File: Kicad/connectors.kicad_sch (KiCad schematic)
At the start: 13 parts, among them J1 Connecteur batterie, J10 HM_10_BLE_Module, J11 DFPlayer_Left, J12 DFPlayer_Right, J14 Speaker, J2 Motor_Left, J3 Motor_Right, J4 Servo_Left, J5 MPU-6050, J6 APDS9960, J7 VL53L0CXV0DH - TOF, J8 Servo_Right, J9 Neopixel

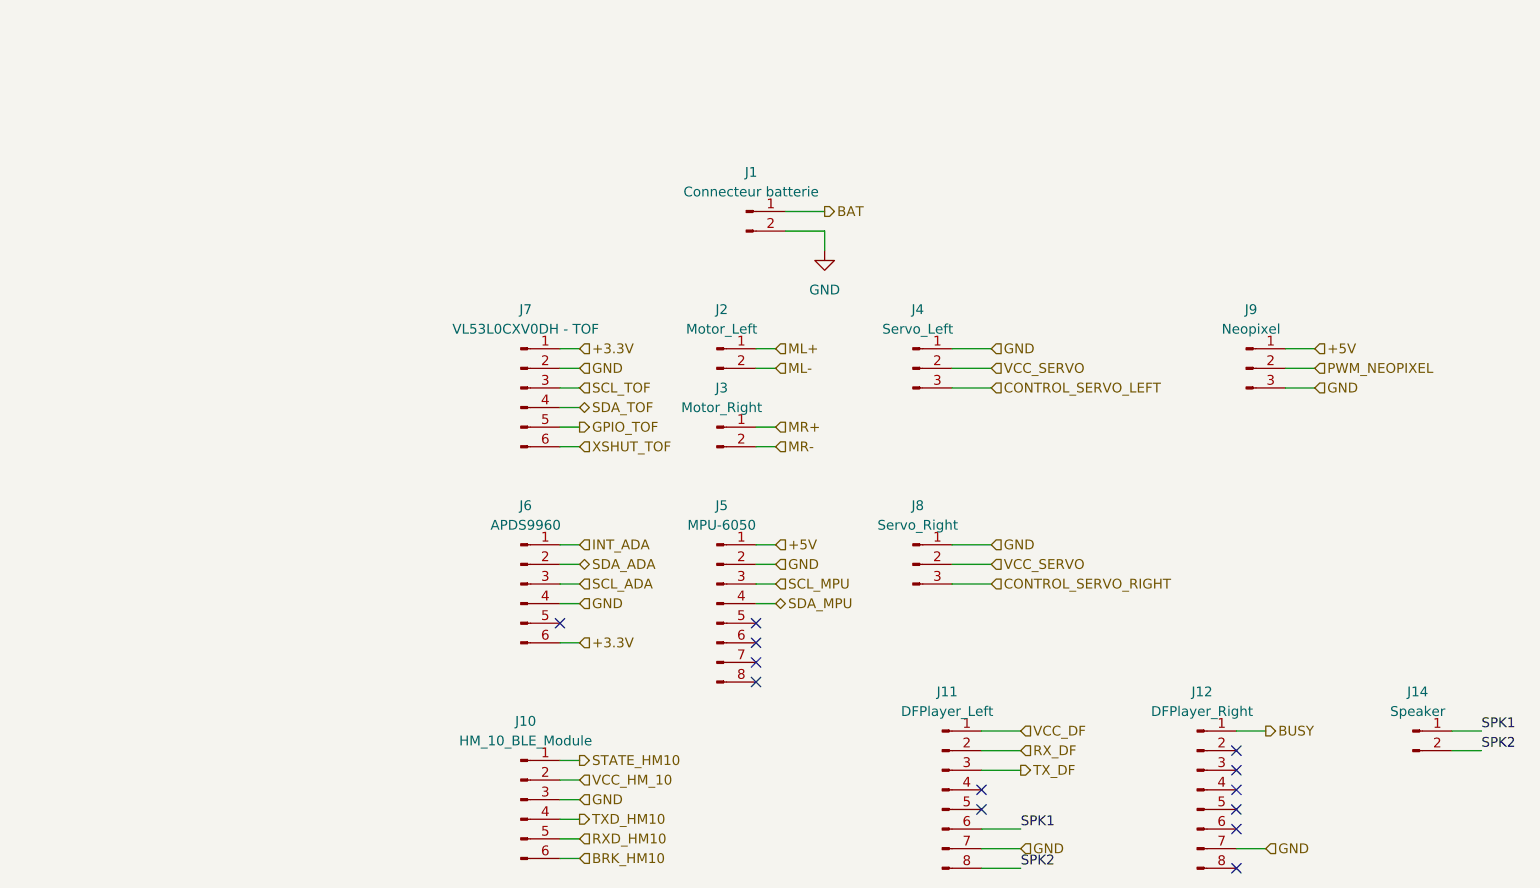
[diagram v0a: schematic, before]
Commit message: Feat: Added power LEDs 5v and 3v, Added Jumpers to battery and bms, Added segmentation in connector sheet, Added encoders, Changed page name from motor diver right to motor driver, Redid annotations, Changed output organisation on stm to match new ioc
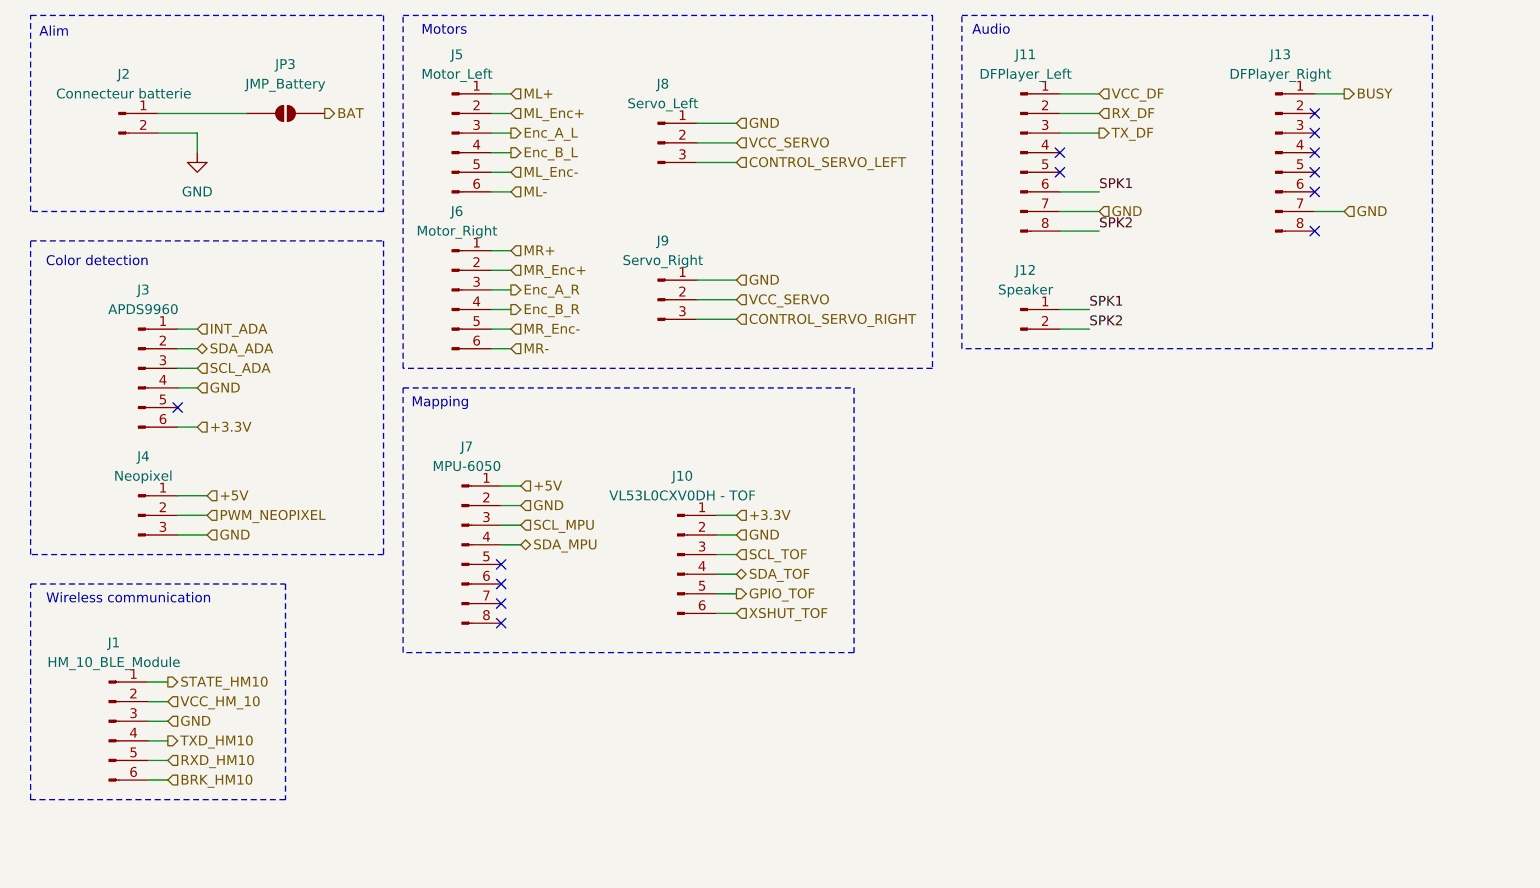
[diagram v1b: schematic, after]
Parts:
- removed J2: Motor_Left, Connector_JST:JST_ZH_B2B-ZR_1x02_P1.50mm_Vertical, symbol Connector:Conn_01x02_Pin
- removed J3: Motor_Right, Connector_JST:JST_ZH_B2B-ZR_1x02_P1.50mm_Vertical, symbol Connector:Conn_01x02_Pin
- added J5: Motor_Left, symbol Connector:Conn_01x06_Pin
- added J6: Motor_Right, symbol Connector:Conn_01x06_Pin
- added JP3: JMP_Battery, symbol Jumper:SolderJumper_2_Open
- renumbered J10 to J1, J7 to J10, J14 to J12, J12 to J13, J1 to J2, J6 to J3, J9 to J4, J5 to J7, J4 to J8, J8 to J9
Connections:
- net BAT: now also JP3.2 (B); no longer J2.1 (Pin_1)
- net ML+: now also J5.1 (Pin_1)
- net ML-: now also J5.6 (Pin_6)
- net MR+: now also J6.1 (Pin_1)
- net MR-: now also J6.6 (Pin_6)
- new net: J2.1 (Pin_1), JP3.1 (A)
- new net Enc_A_L: J5.3 (Pin_3)
- new net Enc_A_R: J6.3 (Pin_3)
- new net Enc_B_L: J5.4 (Pin_4)
- new net Enc_B_R: J6.4 (Pin_4)
- new net ML_Enc+: J5.2 (Pin_2)
- new net ML_Enc-: J5.5 (Pin_5)
- new net MR_Enc+: J6.2 (Pin_2)
- new net MR_Enc-: J6.5 (Pin_5)
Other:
- note added: "Alim"
- note added: "Audio"
- note added: "Color detection"
- note added: "Mapping"
- note added: "Motors"
- note added: "Wireless communication"
- moved on the sheet: J1, J10, J11, J12, J13, J2, J3, J4, J7, J8, J9

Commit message: feat: added the footprints for the solderjumpers
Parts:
- JP3: footprint (none) -> Jumper:SolderJumper-2_P1.3mm_Open_TrianglePad1.0x1.5mm
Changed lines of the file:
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@@
 			)
 		)
-		(property "Footprint" ""
+		(property "Footprint" "Jumper:SolderJumper-2_P1.3mm_Open_TrianglePad1.0x1.5mm"
 			(at 52.07 33.02 0)
 			(hide yes)

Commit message: feat: replaced the footprints of the connectors with fooprints of JST connectors
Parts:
- J10: footprint Connector_PinSocket_2.54mm:PinSocket_1x06_P2.54mm_Vertical -> Connector_JST:JST_XH_S6B-XH-A_1x06_P2.50mm_Horizontal
- J11, J13, J7: footprint Connector_PinSocket_2.54mm:PinSocket_1x08_P2.54mm_Vertical -> Connector_JST:JST_XH_B8B-XH-A_1x08_P2.50mm_Vertical
- J12: footprint Connector_PinSocket_2.54mm:PinSocket_1x02_P2.54mm_Vertical -> Connector_JST:JST_XH_B2B-XH-A_1x02_P2.50mm_Vertical
- J3: footprint Connector_PinSocket_2.54mm:PinSocket_1x06_P2.54mm_Vertical -> Connector_JST:JST_XH_B6B-XH-A_1x06_P2.50mm_Vertical
- J4, J8, J9: footprint Connector_PinHeader_2.54mm:PinHeader_1x03_P2.54mm_Vertical -> Connector_JST:JST_XH_B3B-XH-A_1x03_P2.50mm_Vertical
- J5, J6: footprint (none) -> Connector_JST:JST_XH_B2B-XH-A_1x02_P2.50mm_Vertical
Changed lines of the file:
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@@
 			)
 		)
-		(property "Footprint" "Connector_PinSocket_2.54mm:PinSocket_1x08_P2.54mm_Vertical"
+		(property "Footprint" "Connector_JST:JST_XH_B8B-XH-A_1x08_P2.50mm_Vertical"
 			(at 74.93 88.9 0)
 			(hide yes)
@@
 			)
 		)
-		(property "Footprint" "Connector_PinHeader_2.54mm:PinHeader_1x03_P2.54mm_Vertical"
+		(property "Footprint" "Connector_JST:JST_XH_B3B-XH-A_1x03_P2.50mm_Vertical"
 			(at 100.33 36.83 0)
 			(hide yes)
@@
 			)
 		)
-		(property "Footprint" "Connector_PinSocket_2.54mm:PinSocket_1x08_P2.54mm_Vertical"
+		(property "Footprint" "Connector_JST:JST_XH_B8B-XH-A_1x08_P2.50mm_Vertical"
 			(at 180.34 38.1 0)
 			(hide yes)
@@
 			)
 		)
-		(property "Footprint" "Connector_PinHeader_2.54mm:PinHeader_1x03_P2.54mm_Vertical"
+		(property "Footprint" "Connector_JST:JST_XH_B3B-XH-A_1x03_P2.50mm_Vertical"
 			(at 33.02 85.09 0)
 			(hide yes)
@@
 			)
 		)
-		(property "Footprint" "Connector_PinSocket_2.54mm:PinSocket_1x08_P2.54mm_Vertical"
+		(property "Footprint" "Connector_JST:JST_XH_B8B-XH-A_1x08_P2.50mm_Vertical"
 			(at 147.32 38.1 0)
 			(hide yes)
@@
 			)
 		)
-		(property "Footprint" ""
+		(property "Footprint" "Connector_JST:JST_XH_B2B-XH-A_1x02_P2.50mm_Vertical"
 			(at 73.66 35.56 0)
 			(hide yes)
@@
 			)
 		)
-		(property "Footprint" "Connector_PinSocket_2.54mm:PinSocket_1x06_P2.54mm_Vertical"
+		(property "Footprint" "Connector_JST:JST_XH_B6B-XH-A_1x06_P2.50mm_Vertical"
 			(at 33.02 66.04 0)
 			(hide yes)
@@
 			)
 		)
-		(property "Footprint" "Connector_PinSocket_2.54mm:PinSocket_1x02_P2.54mm_Vertical"
+		(property "Footprint" "Connector_JST:JST_XH_B2B-XH-A_1x02_P2.50mm_Vertical"
 			(at 147.32 58.42 0)
 			(hide yes)
@@
 			)
 		)
-		(property "Footprint" "Connector_PinHeader_2.54mm:PinHeader_1x03_P2.54mm_Vertical"
+		(property "Footprint" "Connector_JST:JST_XH_B3B-XH-A_1x03_P2.50mm_Vertical"
 			(at 100.33 57.15 0)
 			(hide yes)
@@
 			)
 		)
-		(property "Footprint" ""
+		(property "Footprint" "Connector_JST:JST_XH_B2B-XH-A_1x02_P2.50mm_Vertical"
 			(at 73.66 55.88 0)
 			(hide yes)
@@
 			)
 		)
-		(property "Footprint" "Connector_PinSocket_2.54mm:PinSocket_1x06_P2.54mm_Vertical"
+		(property "Footprint" "Connector_JST:JST_XH_S6B-XH-A_1x06_P2.50mm_Horizontal"
 			(at 102.87 90.17 0)
 			(hide yes)

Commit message: feat: changed the footprints to 1206 for the shunt resistors R18 and R19 and put a JST connector footprint for the Bluetooth Module
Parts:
- J1: footprint Connector_PinSocket_2.54mm:PinSocket_1x06_P2.54mm_Vertical -> Connector_JST:JST_XH_S6B-XH-A_1x06_P2.50mm_Horizontal
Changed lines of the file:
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@@
 			)
 		)
-		(property "Footprint" "Connector_PinSocket_2.54mm:PinSocket_1x06_P2.54mm_Vertical"
+		(property "Footprint" "Connector_JST:JST_XH_S6B-XH-A_1x06_P2.50mm_Horizontal"
 			(at 29.21 111.76 0)
 			(hide yes)

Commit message: fix: replaced the fooprints of the connectors of the TOF and Bluetooth Module with vertical ones
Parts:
- J1, J10: footprint Connector_JST:JST_XH_S6B-XH-A_1x06_P2.50mm_Horizontal -> Connector_JST:JST_XH_B6B-XH-A_1x06_P2.50mm_Vertical
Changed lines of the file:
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@@
 			)
 		)
-		(property "Footprint" "Connector_JST:JST_XH_S6B-XH-A_1x06_P2.50mm_Horizontal"
+		(property "Footprint" "Connector_JST:JST_XH_B6B-XH-A_1x06_P2.50mm_Vertical"
 			(at 29.21 111.76 0)
 			(hide yes)
@@
 			)
 		)
-		(property "Footprint" "Connector_JST:JST_XH_S6B-XH-A_1x06_P2.50mm_Horizontal"
+		(property "Footprint" "Connector_JST:JST_XH_B6B-XH-A_1x06_P2.50mm_Vertical"
 			(at 102.87 90.17 0)
 			(hide yes)

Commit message: feat: electrical schematic validated
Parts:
- removed J2: Connecteur batterie, Connector_JST:JST_XH_B2B-XH-A_1x02_P2.50mm_Vertical, symbol Connector:Conn_01x02_Pin
- removed JP3: JMP_Battery, Jumper:SolderJumper-2_P1.3mm_Open_TrianglePad1.0x1.5mm, symbol Jumper:SolderJumper_2_Open
- added C35, C36, C37, C38, C39, C40, C41, C42, C43, C44: 100n, Capacitor_SMD:C_0402_1005Metric, symbol Device:C_Small
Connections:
- net ML_Enc+ is gone; now on net +3.3V: J5.2 (Pin_2)
- net ML_Enc- is gone; now on net GND: J5.5 (Pin_5)
- net MR_Enc+ is gone; now on net +3.3V: J6.2 (Pin_2)
- net MR_Enc- is gone; now on net GND: J6.5 (Pin_5)
- net VCC_DF is gone; now on net +5V: J11.1 (Pin_1)
- net VCC_HM_10 is gone; now on net +5V: J1.2 (Pin_2)
- net VCC_SERVO is gone; now on net +5V: J8.2 (Pin_2), J9.2 (Pin_2)
- net +3.3V: now also C36.2, C39.1, C41.1, C44.1
- net +5V: now also C35.1, C37.1, C38.1, C40.2, C42.2, C43.1
- net GND: now also C35.2, C36.1, C37.2, C38.2, C39.2, C40.1, C41.2, C42.1, C43.2, C44.2
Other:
- note removed: "Alim"
- moved on the sheet: J1, J3, J4

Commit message: feat: added the footprints for new components and started assigning the JLCPCB part numbers
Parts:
- C35, C36, C37, C38, C39, C40, C41, C42, C43, C44: JLCPCB Part # (none) -> C1525
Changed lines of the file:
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@@
 			)
 		)
+		(property "JLCPCB Part #" "C1525"
+			(at 166.37 41.91 0)
+			(hide yes)
+			(show_name no)
+			(do_not_autoplace no)
+			(effects
+				(font
+					(size 1.27 1.27)
+				)
+			)
+		)
 		(pin "1"
 		)
@@
 			)
 		)
+		(property "JLCPCB Part #" "C1525"
+			(at 92.71 36.83 0)
+			(hide yes)
+			(show_name no)
+			(do_not_autoplace no)
+			(effects
+				(font
+					(size 1.27 1.27)
+				)
+			)
+		)
 		(pin "1"
 		)
@@
 			)
 		)
+		(property "JLCPCB Part #" "C1525"
+			(at 92.71 57.15 0)
+			(hide yes)
+			(show_name no)
+			(do_not_autoplace no)
+			(effects
+				(font
+					(size 1.27 1.27)
+				)
+			)
+		)
 		(pin "1"
 		)
@@
 			)
 		)
+		(property "JLCPCB Part #" "C1525"
+			(at 124.46 87.63 0)
+			(hide yes)
+			(show_name no)
+			(do_not_autoplace no)
+			(effects
+				(font
+					(size 1.27 1.27)
+				)
+			)
+		)
 		(pin "1"
 		)
@@
 			)
 		)
+		(property "JLCPCB Part #" "C1525"
+			(at 35.56 41.91 0)
+			(hide yes)
+			(show_name no)
+			(do_not_autoplace no)
+			(effects
+				(font
+					(size 1.27 1.27)
+				)
+			)
+		)
 		(pin "1"
 		)
@@
 			)
 		)
+		(property "JLCPCB Part #" "C1525"
+			(at 53.34 83.82 0)
+			(hide yes)
+			(show_name no)
+			(do_not_autoplace no)
+			(effects
+				(font
+					(size 1.27 1.27)
+				)
+			)
+		)
 		(pin "1"
 		)
@@
 			)
 		)
+		(property "JLCPCB Part #" "C1525"
+			(at 111.6439 54.61 0)
+			(hide yes)
+			(show_name no)
+			(do_not_autoplace no)
+			(effects
+				(font
+					(size 1.27 1.27)
+				)
+			)
+		)
 		(pin "1"
 		)
@@
 			)
 		)
+		(property "JLCPCB Part #" "C1525"
+			(at 83.82 81.28 0)
+			(hide yes)
+			(show_name no)
+			(do_not_autoplace no)
+			(effects
+				(font
+					(size 1.27 1.27)
+				)
+			)
+		)
 		(pin "1"
 		)
@@
 			)
 		)
+		(property "JLCPCB Part #" "C1525"
+			(at 114.3 34.29 90)
+			(hide yes)
+			(show_name no)
+			(do_not_autoplace no)
+			(effects
+				(font
+					(size 1.27 1.27)
+				)
+			)
+		)
 		(pin "1"
 		)
@@
 			(hide yes)
 			(show_name no)
+			(do_not_autoplace no)
+			(effects
+				(font
+					(size 1.27 1.27)
+				)
+			)
+		)
+		(property "JLCPCB Part #" "C1525"
+			(at 53.34 55.88 0)
+			(hide yes)
+			(show_name no)

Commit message: Feat: Placed components on wiring schematic, chore: fixed footprint names and values
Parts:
- J11, J13, J7: footprint Connector_JST:JST_XH_B8B-XH-A_1x08_P2.50mm_Vertical -> Connector_PinSocket_2.54mm:PinSocket_1x08_P2.54mm_Vertical
- J5, J6: footprint Connector_JST:JST_XH_B2B-XH-A_1x02_P2.50mm_Vertical -> Connector_JST:JST_XH_B6B-XH-AM_1x06_P2.50mm_Vertical
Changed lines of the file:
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@@
 			)
 		)
-		(property "Footprint" "Connector_JST:JST_XH_B8B-XH-A_1x08_P2.50mm_Vertical"
+		(property "Footprint" "Connector_PinSocket_2.54mm:PinSocket_1x08_P2.54mm_Vertical"
 			(at 74.93 88.9 0)
 			(hide yes)
@@
 			)
 		)
-		(property "Footprint" "Connector_JST:JST_XH_B8B-XH-A_1x08_P2.50mm_Vertical"
+		(property "Footprint" "Connector_PinSocket_2.54mm:PinSocket_1x08_P2.54mm_Vertical"
 			(at 180.34 38.1 0)
 			(hide yes)
@@
 			)
 		)
-		(property "Footprint" "Connector_JST:JST_XH_B8B-XH-A_1x08_P2.50mm_Vertical"
+		(property "Footprint" "Connector_PinSocket_2.54mm:PinSocket_1x08_P2.54mm_Vertical"
 			(at 147.32 38.1 0)
 			(hide yes)
@@
 			)
 		)
-		(property "Footprint" "Connector_JST:JST_XH_B2B-XH-A_1x02_P2.50mm_Vertical"
+		(property "Footprint" "Connector_JST:JST_XH_B6B-XH-AM_1x06_P2.50mm_Vertical"
 			(at 73.66 35.56 0)
 			(hide yes)
@@
 			)
 		)
-		(property "Footprint" "Connector_JST:JST_XH_B2B-XH-A_1x02_P2.50mm_Vertical"
+		(property "Footprint" "Connector_JST:JST_XH_B6B-XH-AM_1x06_P2.50mm_Vertical"
 			(at 73.66 55.88 0)
 			(hide yes)
